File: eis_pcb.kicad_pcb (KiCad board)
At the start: 4 copper layers, 33 x 34.7 mm, 49 parts, among them J1 Conn_01x01_Socket, J12 104031-0811, J13 10051922-1810ELF, J2 GSB1C41110SSHR, J3 Conn_01x01_Socket, J7 Conn_01x02_Socket, Q3 IRLML6344TRPBF, U1 AD5941BCPZ, U3 ESP32-S3-WROOM-1-N8R8, U4 MCP73831T-2DCI_OT, U5 NCP186AMX330TAG

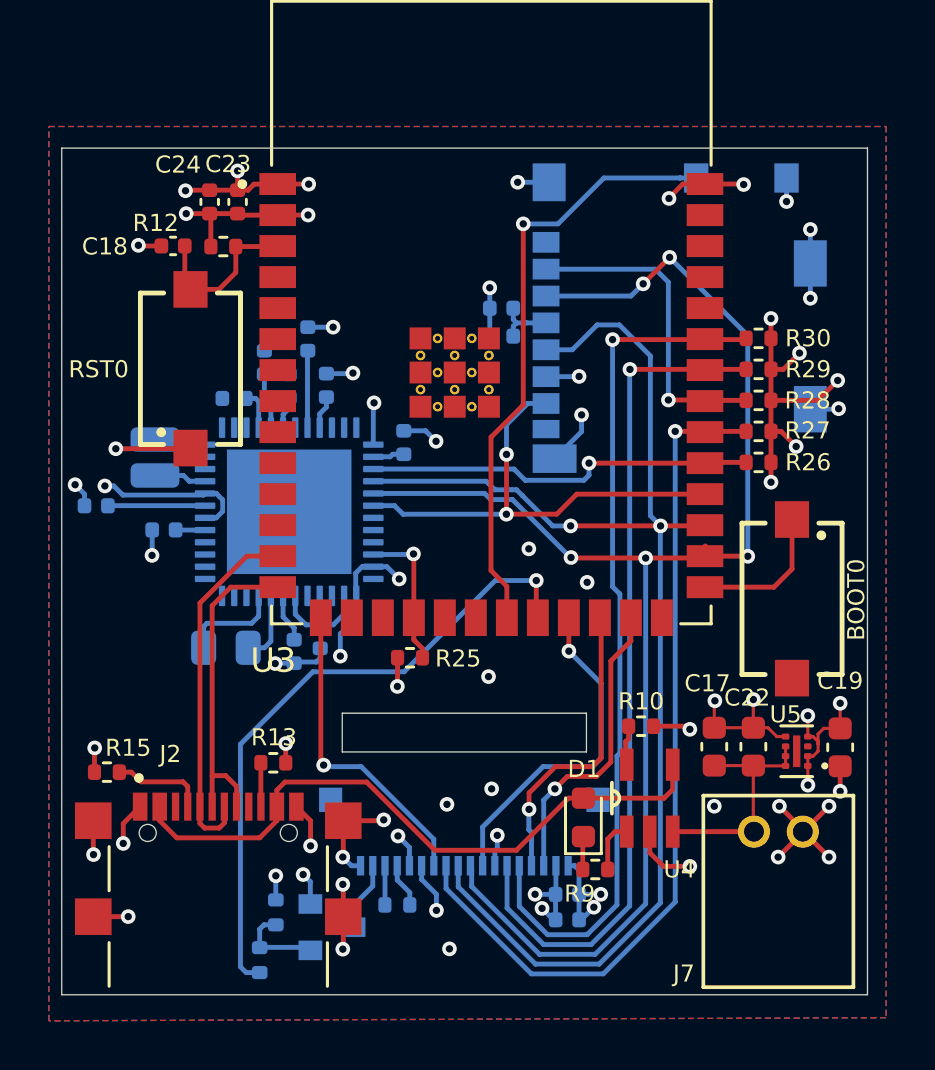
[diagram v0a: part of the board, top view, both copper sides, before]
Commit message: Finished PCB with manufacturing files in production folder
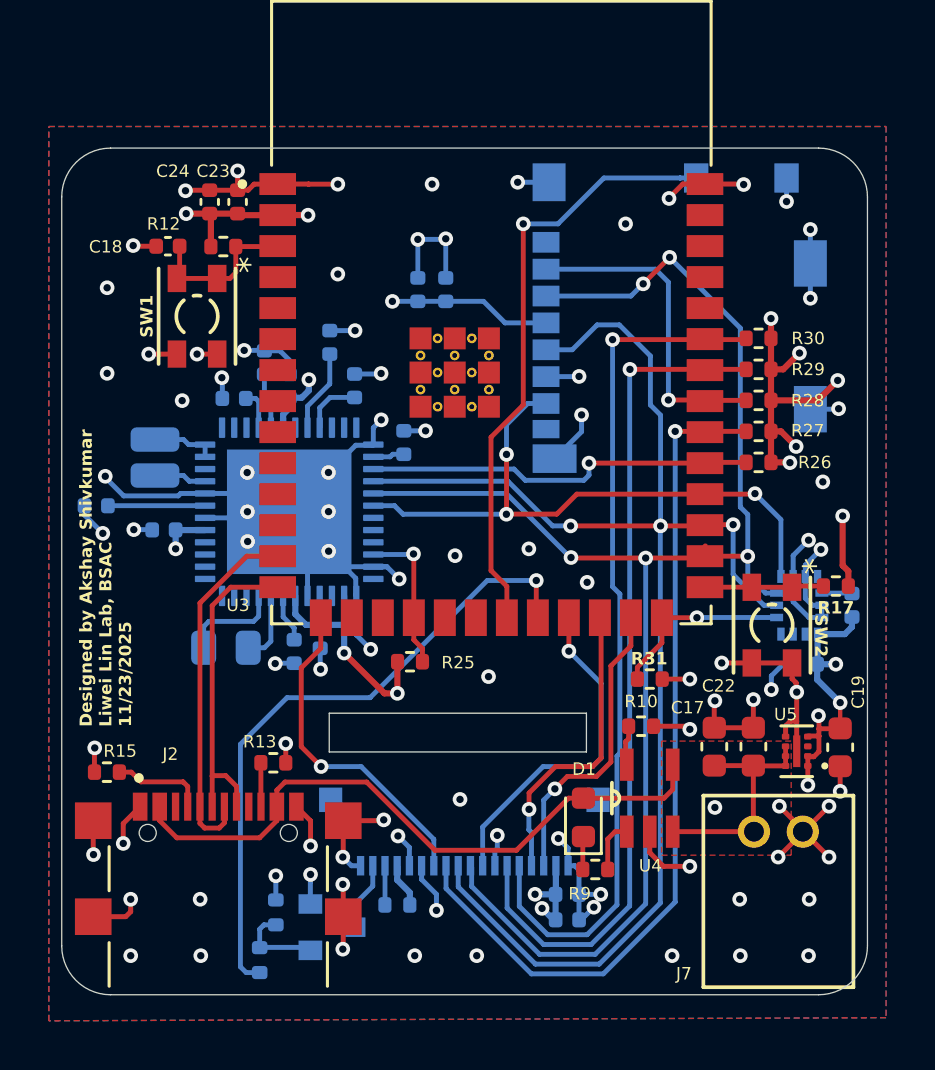
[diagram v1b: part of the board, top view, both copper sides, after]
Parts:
- removed BOOT0, RST0: B3U-1100PM, 434121025816:434121025816
- added C25: 100nF, Capacitor_SMD:C_0402_1005Metric, B.Cu at (139.7, 114.4)
- added C26: 100nF, Capacitor_SMD:C_0402_1005Metric, B.Cu at (141.6, 112.0)
- added R17: 10k, Resistor_SMD:R_0402_1005Metric, F.Cu at (140.9, 111.2)
- added R31: 4.7k, Resistor_SMD:R_0402_1005Metric, F.Cu at (133.3, 115.0)
- added SW1: SW_Push_Dual, SWITCH_0SMTRLFS-L:SWITCH_0SMTRLFS-L, F.Cu at (114.8, 100.2)
- added SW2: SW_Push_Dual, SWITCH_0SMTRLFS-L:SWITCH_0SMTRLFS-L, F.Cu at (138.3, 112.8)
- added U2: LSM6DSVTR, LSM6DSVTR:LGA14-L_2P59X3P1X0P5_STM, B.Cu at (139.4, 112.0)
- moved C11 3.92 mm to (123.8, 99.1), turned to 90 degrees
- moved C12 2.41 mm to (125.0, 99.1), turned to 90 degrees
- moved C10 1.15 mm to (121.2, 103.0)
- moved C9 0.91 mm to (120.2, 101.2)
- moved C18 0.21 mm to (113.6, 97.3)
- moved R25 0.16 mm to (123.5, 114.3)
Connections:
- U3 pad 16: /CS.SCREEN -> unconnected-(U3-IO46-Pad16)
- U3 pad 26: unconnected-(U3-IO45-Pad26) -> /CS.IMU
- U3 pad 32: unconnected-(U3-IO39-Pad32) -> /CS.SCREEN
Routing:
- net GND: track 90.0 -> 143.1 mm, vias 58 -> 91
- net +3V3: track 40.4 -> 60.9 mm, vias 13 -> 20
- net /CS.IMU: track 0.00 -> 7.63 mm, vias 0 -> 1
- net /MISO: track 19.7 -> 25.6 mm, vias 2 -> 3
- net /SCLK: track 54.1 -> 59.6 mm, vias 2 -> 3
- net /MOSI: track 60.0 -> 62.3 mm
- net Net-(U2-VDD_IO): track 0.00 -> 1.24 mm
- net /ZERO.0: track 1.37 -> 2.42 mm
- net /BOOT: track 5.90 -> 4.87 mm
- net /DC: track 12.9 -> 13.7 mm
- added copper zone on In2.Cu, net +3V3
- added copper zone on F.Cu, net +BATT
- added copper zone on In1.Cu, net GND
- removed copper zone on In1.Cu, net +3V3
- removed copper zone on In2.Cu, net GND
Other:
- outline, holes or cut-outs redrawn
- board text added: "Designed by Akshay Shivkumar Liwei Lin Lab, BSAC 11/23/2025"

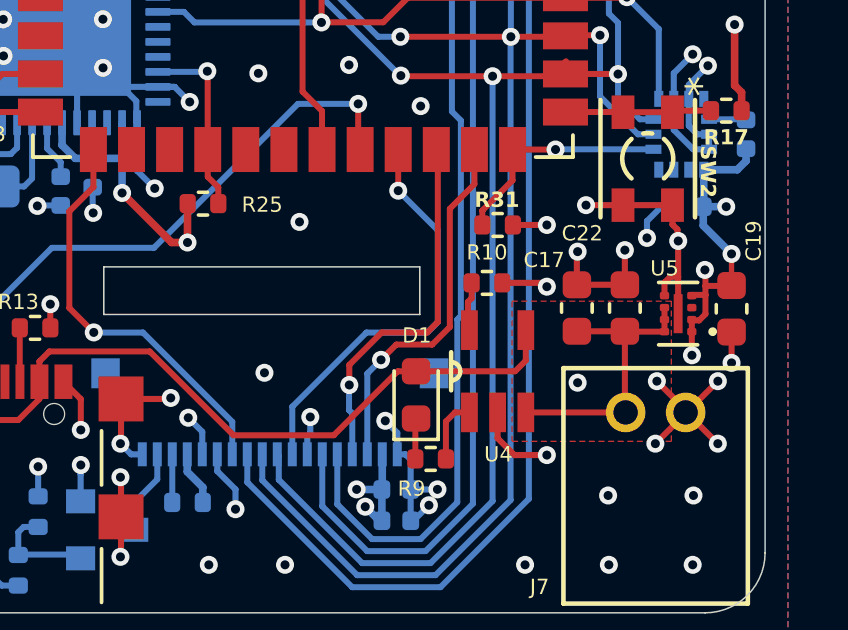
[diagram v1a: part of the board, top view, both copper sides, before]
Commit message: Removed battery zone
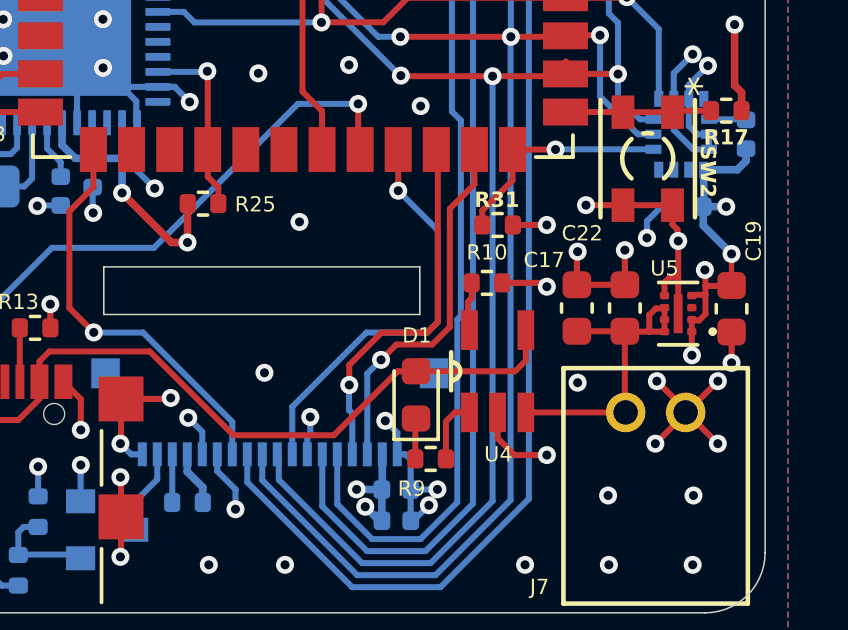
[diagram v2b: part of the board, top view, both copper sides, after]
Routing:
- net +BATT: track 9.85 -> 11.0 mm
- removed copper zone on F.Cu, net +BATT
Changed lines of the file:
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@@
 		(tags "resistor")
 		(property "Reference" "R25"
-			(at -1.9718 -0.036 180)
+			(at -1.7432 -0.0254 180)
 			(layer "F.SilkS")
 			(effects
@@
 	)
 	(segment
+		(start 138.3792 118.0338)
+		(end 138.5944 117.8186)
+		(width 0.2)
+		(layer "F.Cu")
+		(net 11)
+	)
+	(segment
 		(start 138.8872 118.1926)
 		(end 138.8872 118.5926)
@@
 	)
 	(segment
+		(start 138.3792 118.5926)
+		(end 137.5788 118.5926)
+		(width 0.2)
+		(layer "F.Cu")
+		(net 11)
+	)
+	(segment
 		(start 137.5664 121.2596)
 		(end 137.5918 121.285)
@@
 	)
 	(segment
+		(start 138.5944 117.8186)
+		(end 138.8872 117.8186)
+		(width 0.2)
+		(layer "F.Cu")
+		(net 11)
+	)
+	(segment
 		(start 138.8872 118.5926)
-		(end 137.5788 118.5926)
+		(end 138.3792 118.5926)
 		(width 0.2)
 		(layer "F.Cu")
@@
 	)
 	(segment
+		(start 138.3792 118.5926)
+		(end 138.3792 118.0338)
+		(width 0.2)
+		(layer "F.Cu")
+		(net 11)
+	)
+	(segment
 		(start 134.1882 121.285)
 		(end 137.5918 121.285)
@@
 	)
 	(zone
-		(net 11)
-		(net_name "+BATT")
-		(layer "F.Cu")
-		(hatch edge 0.5)
-		(priority 1)
-		(connect_pads
-			(clearance 0.5)
-		)
-		(min_thickness 0.25)
-		(filled_areas_thickness no)
-		(fill yes
-			(thermal_gap 0.5)
-			(thermal_bridge_width 0.5)
-		)
-		(polygon
-			(pts
-				(xy 139.1158 117.5766) (xy 133.8072 117.5766) (xy 133.8072 122.2502) (xy 139.1158 122.2502)
-			)
-		)
-	)
-	(zone

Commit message: Final PCB
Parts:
- U2: value LSM6DSVTR -> LGA14-L_2P59X3P1X0P5_STM; footprint LSM6DSVTR:LGA14-L_2P59X3P1X0P5_STM -> LSM6DSVTR:LGA14-L_2P59X3P1X0P5_STM-L
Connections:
- U2 pad 1: /MISO -> (no net)
- U2 pad 10: unconnected-(U2-OCS_AUX-Pad10) -> (no net)
- U2 pad 11: unconnected-(U2-SDO_AUX-Pad11) -> (no net)
- U2 pad 12: /CS.IMU -> (no net)
- U2 pad 13: /SCLK -> (no net)
- U2 pad 14: /MOSI -> (no net)
- U2 pad 2: GND -> (no net)
- U2 pad 3: GND -> (no net)
- U2 pad 4: unconnected-(U2-INT1-Pad4) -> (no net)
- U2 pad 5: Net-(U2-VDD_IO) -> (no net)
- U2 pad 6: GND -> (no net)
- U2 pad 7: GND -> (no net)
- U2 pad 8: +3V3 -> (no net)
- U2 pad 9: unconnected-(U2-INT2-Pad9) -> (no net)

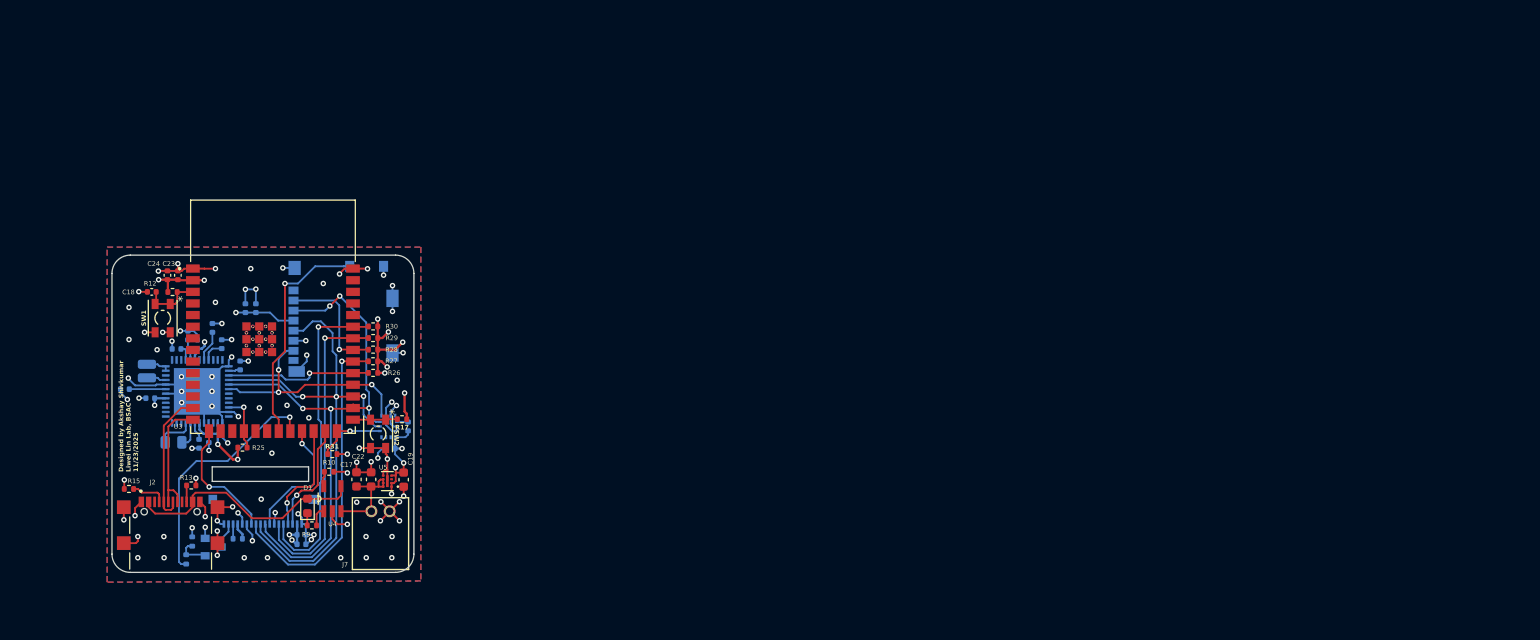
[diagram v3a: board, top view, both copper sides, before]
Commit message: complete noise suppression, begin layout
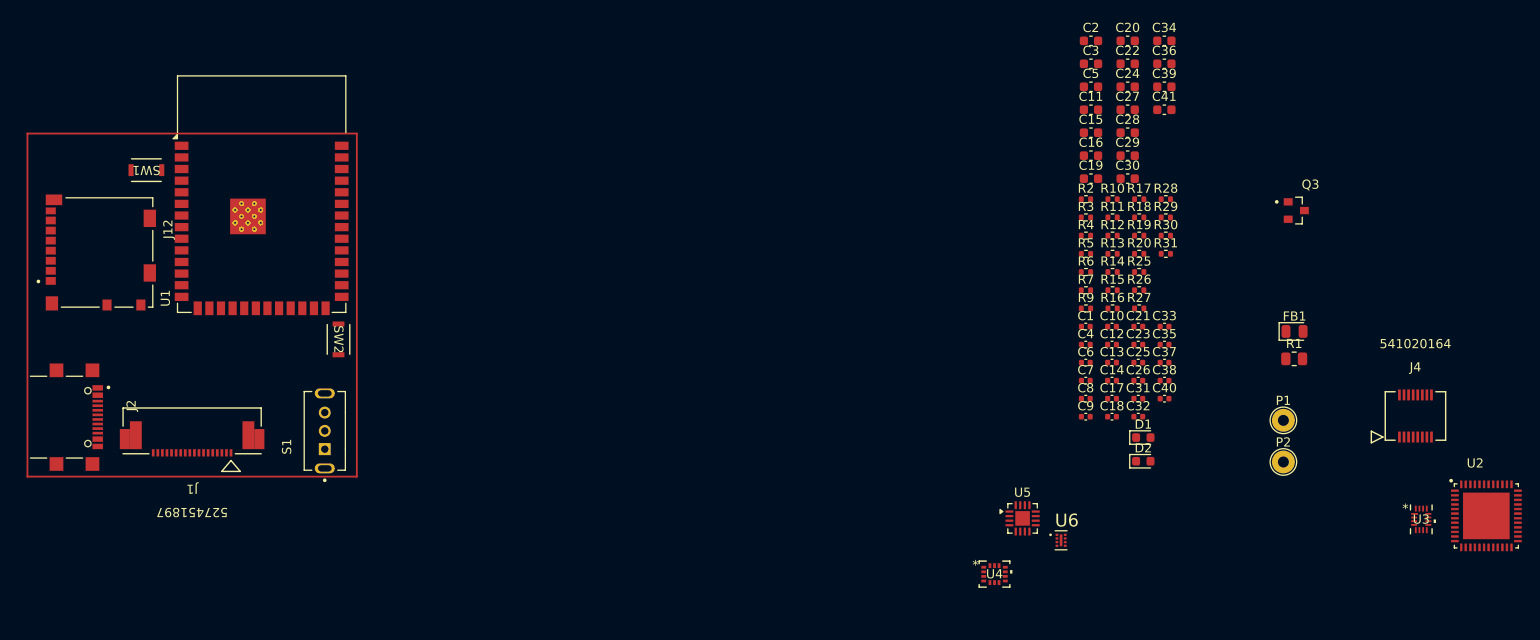
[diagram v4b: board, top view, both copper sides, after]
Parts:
- removed J13: 10051922-1810ELF, 10051922-1810ELF:AMPHENOL_10051922-1810ELF
- removed J3: Conn_01x01_Socket, Connector_Wire:SolderWirePad_1x01_SMD_1x2mm
- removed J7: Conn_01x02_Socket, S2B_PH_K_S_LF__SN_:CONN_S2B-PH-K-S_JST
- added C13: 100n, Capacitor_SMD:C_0402_1005Metric, F.Cu at (218.5, 105.0)
- added C14: 100n, Capacitor_SMD:C_0402_1005Metric, F.Cu at (218.5, 107.0)
- added C15: 1u, Capacitor_SMD:C_0603_1608Metric, F.Cu at (216.2, 79.9)
- added C16: 1u, Capacitor_SMD:C_0603_1608Metric, F.Cu at (216.2, 82.4)
- added C27: 1u, Capacitor_SMD:C_0603_1608Metric, F.Cu at (220.3, 77.4)
- added C28: 4.7u, Capacitor_SMD:C_0603_1608Metric, F.Cu at (220.3, 79.9)
- added C29: 4.7u, Capacitor_SMD:C_0603_1608Metric, F.Cu at (220.3, 82.4)
- added C30: 10u, Capacitor_SMD:C_0603_1608Metric, F.Cu at (220.3, 84.9)
- added C31: 100n, Capacitor_SMD:C_0402_1005Metric, F.Cu at (221.4, 109.0)
- added C32: 100n, Capacitor_SMD:C_0402_1005Metric, F.Cu at (221.4, 110.9)
- added C33: 100n, Capacitor_SMD:C_0402_1005Metric, F.Cu at (224.3, 101.1)
- added C34: 10u, Capacitor_SMD:C_0603_1608Metric, F.Cu at (224.3, 69.9)
- added C35: 100n, Capacitor_SMD:C_0402_1005Metric, F.Cu at (224.3, 103.1)
- added C36: 1u, Capacitor_SMD:C_0603_1608Metric, F.Cu at (224.3, 72.4)
- added C37: 100n, Capacitor_SMD:C_0402_1005Metric, F.Cu at (224.3, 105.0)
- added C38: 100n, Capacitor_SMD:C_0402_1005Metric, F.Cu at (224.3, 107.0)
- added C39: 1u, Capacitor_SMD:C_0603_1608Metric, F.Cu at (224.3, 74.9)
- added C40: 100n, Capacitor_SMD:C_0402_1005Metric, F.Cu at (224.3, 109.0)
- added C41: 1u, Capacitor_SMD:C_0603_1608Metric, F.Cu at (224.3, 77.4)
- added D2: USB, LED_SMD:LED_0603_1608Metric, F.Cu at (222.0, 115.8)
- added FB1: 600R@100MHz, Diode_SMD:D_0805_2012Metric, F.Cu at (238.5, 101.6)
- added J4: 541020164, 541020164:CON_541020164, F.Cu at (251.7, 110.9)
- added P1: V.BATT, TestPoint:TestPoint_THTPad_D2.5mm_Drill1.2mm, F.Cu at (237.3, 111.3)
- added P2: GND.BATT, TestPoint:TestPoint_THTPad_D2.5mm_Drill1.2mm, F.Cu at (237.3, 115.9)
- added R11: 10k, Resistor_SMD:R_0402_1005Metric, F.Cu at (218.6, 89.2)
- added R18: 5.9k, Resistor_SMD:R_0402_1005Metric, F.Cu at (221.5, 89.2)
- added R19: 1.62k, Resistor_SMD:R_0402_1005Metric, F.Cu at (221.5, 91.2)
- added R20: 100k, Resistor_SMD:R_0402_1005Metric, F.Cu at (221.5, 93.1)
- added R3: 220k, Resistor_SMD:R_0402_1005Metric, F.Cu at (215.7, 89.2)
- added R4: 220k, Resistor_SMD:R_0402_1005Metric, F.Cu at (215.7, 91.2)
- added R5: 100k, Resistor_SMD:R_0402_1005Metric, F.Cu at (215.7, 93.1)
- added R6: 2.2R, Resistor_SMD:R_0402_1005Metric, F.Cu at (215.7, 95.1)
- added R7: 2.2R, Resistor_SMD:R_0402_1005Metric, F.Cu at (215.7, 97.1)
- added S1: PWR, SLW_864587_2A_RA_N_D:SW_SLW-864587-2A-RA-N-D, F.Cu at (132.5, 112.5)
- added U6: NCP186AMX330TAG, NCP186AMX330TAG:PSON40P160X120X45-9N, F.Cu at (213.0, 124.5)
- C1, C10, C4, C6, C7, C8, C9, J12, Q3, R1, R14, R16, R2: moved to F.Cu
- C11: value 10uF -> 10u; footprint Capacitor_SMD:C_0402_1005Metric -> Capacitor_SMD:C_0603_1608Metric; moved to F.Cu
- C12, C25, C26: value 100nF -> 100n; moved to F.Cu
- C17: value 10uF -> 100n; footprint Capacitor_SMD:C_0603_1608Metric -> Capacitor_SMD:C_0402_1005Metric
- C18: value 10uF -> 100n
- C19, C23: value 1uF -> 100n
- C2: value 100n -> 1u; footprint Capacitor_SMD:C_0402_1005Metric -> Capacitor_SMD:C_0603_1608Metric; moved to F.Cu
- C20: value 4.7uF -> 4.7u; footprint Capacitor_SMD:C_0402_1005Metric -> Capacitor_SMD:C_0603_1608Metric; moved to F.Cu
- C21: value 0.1uF -> 100n; moved to F.Cu
- C22: value 1uF -> 1u
- C24: value 1uF -> 22u; footprint Capacitor_SMD:C_0402_1005Metric -> Capacitor_SMD:C_0603_1608Metric
- C3: value 100n -> 10u; footprint Capacitor_SMD:C_0402_1005Metric -> Capacitor_SMD:C_0603_1608Metric; moved to F.Cu
- C5: footprint Capacitor_SMD:C_0402_1005Metric -> Capacitor_SMD:C_0603_1608Metric; moved to F.Cu
- D1: value LED -> CHG
- J1: value Conn_01x01_Socket -> 527451897; footprint Connector_Wire:SolderWirePad_1x01_SMD_1x2mm -> 527451897:CON_527451897_MOL; moved to F.Cu
- R10, R9: value 4.7k -> 1.5k
- SW1: value SW_Push_Dual -> RST; footprint SWITCH_0SMTRLFS-L:SWITCH_0SMTRLFS-L -> R_667995:R-667995_MIT
- SW2: value SW_Push_Dual -> BOOT; footprint SWITCH_0SMTRLFS-L:SWITCH_0SMTRLFS-L -> R_667995:R-667995_MIT
- U1: value AD5941BCPZ -> ESP32-S3-WROOM-1-N8R8; footprint AD5941BCPZ:QFN50P700X700X80-49N -> RF_Module:ESP32-S3-WROOM-1; moved to F.Cu
- U2: value LGA14-L_2P59X3P1X0P5_STM -> AD5941BCPZ; footprint LSM6DSVTR:LGA14-L_2P59X3P1X0P5_STM-L -> AD5941BCPZ:QFN50P700X700X80-49N; moved to F.Cu
- U3: value ESP32-S3-WROOM-1-N8R8 -> TMUX1109RSVR; footprint ESP32-S3-WROOM-1-N8R8:XCVR_ESP32S3WROOM1N8R8 -> TMUX1109RSVR:RSV16_TEX
- U4: value MCP73831T-2DCI_OT -> LSM6DSVTR; footprint MCP73831T-2DCI_OT:SOT95P270X145-5N -> LSM6DSVTR:LGA14-L_2P59X3P1X0P5_STM
- U5: value NCP186AMX330TAG -> BQ24075RGT; footprint NCP186AMX330TAG:PSON40P160X120X45-9N -> Package_DFN_QFN:VQFN-16-1EP_3x3mm_P0.5mm_EP1.6x1.6mm
- moved U3 127.5 mm to (252.3, 122.2)
- moved Q3 124.0 mm to (238.7, 88.4)
- moved R1 122.8 mm to (238.5, 104.6), turned to 0 degrees
- moved U2 120.4 mm to (259.5, 121.8), turned to 0 degrees
- moved C5 110.6 mm to (216.2, 74.9), turned to 0 degrees
- moved R15 109.7 mm to (218.6, 97.1), turned to 0 degrees
- moved C3 109.1 mm to (216.2, 72.4), turned to 0 degrees
- moved C24 107.0 mm to (220.3, 74.9), turned to 0 degrees
- moved R2 105.9 mm to (215.7, 87.2), turned to 0 degrees
- moved C18 105.8 mm to (218.5, 110.9), turned to 0 degrees
- moved C20 105.8 mm to (220.3, 69.9)
- moved C2 105.8 mm to (216.2, 69.9), turned to 0 degrees
- moved C23 105.2 mm to (221.4, 103.1), turned to 0 degrees
- moved R14 104.8 mm to (218.6, 95.1), turned to 0 degrees
- moved R13 103.8 mm to (218.6, 93.1)
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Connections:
- C1 pad 1: +3V3 -> Net-(C1-Pad1)
- C17 pad 1: +BATT -> Net-(U2-DVDD)
- C18 pad 1: /MCU.RST -> /RST.MCU
- C2 pad 1: +3V3 -> Net-(C1-Pad1)
- C22 pad 1: +BATT -> +VSYS
- C26 pad 2: Net-(U2-VDD_IO) -> GND
- C3 pad 1: +3V3 -> Net-(C1-Pad1)
- D1 pad 2: +5V -> Net-(D1-A)
- J1 pad 1: /RE -> GND
- Q3 pad 3: /K -> Net-(Q3-Pad3)
- R1 pad 1: Net-(U1-RCAL0) -> Net-(U2-RCAL0)
- R1 pad 2: Net-(U1-RCAL1) -> Net-(U2-RCAL1)
- R10 pad 1: GND -> Net-(D2-A)
- R10 pad 2: Net-(U4-PROG) -> +VSYS
- R12 pad 2: /MCU.RST -> /RST.MCU
- R16 pad 1: +3V3 -> Net-(Q3-Pad3)
- R16 pad 2: Net-(J13-Pad3) -> /K
- R2 pad 1: /ESP.PWM -> /PWM.SCREEN
- R25 pad 1: /AFE.RST -> /RST.AFE
- R27 pad 1: /CS.SCREEN -> Net-(U1-IO39)
- R29 pad 1: /CTP_SCL -> Net-(U1-IO41)
- R30 pad 1: /CTP_SDA -> Net-(U1-IO42)
- R9 pad 1: Net-(D1-K) -> +VSYS
- R9 pad 2: Net-(U4-STAT) -> Net-(D1-A)
- U1 pad 1: unconnected-(U1-RC0_2-Pad1) -> GND
- U1 pad 13: GND -> /DATA-
- U1 pad 14: /DVDD.1V8 -> /DATA+
- U1 pad 15: /CS.AFE -> /SCL.TOUCH
- U1 pad 16: /SCLK -> unconnected-(U1-IO46-Pad16)
- U1 pad 17: /MOSI -> /RST.SCREEN
- U1 pad 18: /MISO -> /CS.SCREEN
- U1 pad 19: unconnected-(U1-GPIO0-Pad19) -> /MOSI.SCREEN
- U1 pad 2: unconnected-(U1-RC0_1-Pad2) -> +3V3
- U1 pad 20: unconnected-(U1-GPIO1-Pad20) -> /SCLK.SCREEN
- U1 pad 21: unconnected-(U1-GPIO2-Pad21) -> /DC.SCREEN
- U1 pad 22: /AFE.RST -> unconnected-(U1-IO14-Pad22)
- U1 pad 23: GND -> /SCREEN.RST
- U1 pad 24: unconnected-(U1-DNC-Pad24) -> /CTP_RST
- U1 pad 25: GND -> /CTP_INT
- U1 pad 26: +3V3 -> /CS.IMU
- U1 pad 27: unconnected-(U1-AFE3-Pad27) -> /BOOT
- U1 pad 29: GND -> unconnected-(U1-IO36-Pad29)
- U1 pad 3: unconnected-(U1-RC0_0-Pad3) -> /RST.MCU
- U1 pad 30: +3V3 -> unconnected-(U1-IO37-Pad30)
- U1 pad 31: /BIAS.CAP -> unconnected-(U1-IO38-Pad31)
- U1 pad 32: Net-(U1-RCAL0) -> Net-(U1-IO39)
- U1 pad 33: Net-(U1-RCAL1) -> /CS.SD
- U1 pad 34: unconnected-(U1-AFE1-Pad34) -> Net-(U1-IO41)
- U1 pad 35: unconnected-(U1-AFE2-Pad35) -> Net-(U1-IO42)
- U1 pad 4: /REF.2V5 -> unconnected-(U1-IO4-Pad4)
- U1 pad 40: unconnected-(U1-AIN4/LPF0-Pad40) -> GND
- U1 pad 41: +3V3 -> (no net)
- U1 pad 5: /AVDD.REG -> unconnected-(U1-IO5-Pad5)
- U1 pad 6: +3V3 -> unconnected-(U1-IO6-Pad6)
- U1 pad 8: /BIAS.0 -> unconnected-(U1-IO15-Pad8)
- U1 pad 9: /ZERO.0 -> unconnected-(U1-IO16-Pad9)
- U2 pad 1: (no net) -> unconnected-(U2-RC0_2-Pad1)
- U2 pad 10: (no net) -> unconnected-(U2-DNC-Pad10)
- U2 pad 11: (no net) -> unconnected-(U2-XTALI-Pad11)
- U2 pad 12: (no net) -> unconnected-(U2-XTALO-Pad12)
- U2 pad 13: (no net) -> GND
- U2 pad 14: (no net) -> /DVDD.1V8
- U2 pad 2: (no net) -> unconnected-(U2-RC0_1-Pad2)
- U2 pad 3: (no net) -> unconnected-(U2-RC0_0-Pad3)
- U2 pad 4: (no net) -> /REF.2V5
- U2 pad 5: (no net) -> /AVDD.REG
- U2 pad 6: (no net) -> Net-(U2-DVDD)
- U2 pad 7: (no net) -> unconnected-(U2-DNC-Pad7)
- U2 pad 8: (no net) -> /BIAS.0
- U2 pad 9: (no net) -> /ZERO.0
- U3 pad 10: unconnected-(U3-IO17-Pad10) -> /WE2
- U3 pad 11: unconnected-(U3-IO18-Pad11) -> /WE1
- U3 pad 12: unconnected-(U3-IO8-Pad12) -> /3V3A
- U3 pad 13: /DATA- -> GND
- U3 pad 14: /DATA+ -> /A1.MUX
- U3 pad 15: /DC -> /A0.MUX
- U3 pad 16: unconnected-(U3-IO46-Pad16) -> /EN.MUX
- U3 pad 2: +3V3 -> /CE1
- U3 pad 3: /MCU.RST -> /CE2
- U3 pad 4: unconnected-(U3-IO4-Pad4) -> /CE3
- U3 pad 5: unconnected-(U3-IO5-Pad5) -> /CE4
- U3 pad 6: unconnected-(U3-IO6-Pad6) -> /CE0
- U3 pad 7: unconnected-(U3-IO7-Pad7) -> /WE0
- U3 pad 8: unconnected-(U3-IO15-Pad8) -> /WE4
- U3 pad 9: unconnected-(U3-IO16-Pad9) -> /WE3
- U4 pad 1: Net-(U4-STAT) -> /MISO
- U4 pad 3: +BATT -> GND
- U4 pad 4: +5V -> /INT.IMU
- U4 pad 5: Net-(U4-PROG) -> +3V3
- U5 pad 1: +3V3 -> Net-(U5-TS)
- U5 pad 2: +3V3 -> +BATT
- U5 pad 3: unconnected-(U5-N/C-Pad3) -> +BATT
- U5 pad 4: +3V3 -> GND
- U5 pad 5: GND -> +VSYS
- U5 pad 6: +BATT -> GND
- U5 pad 7: +BATT -> Net-(D2-K)
- U5 pad 8: +BATT -> GND
- U5 pad 9: GND -> Net-(D1-K)
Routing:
- net GND: track 143.1 -> 0.00 mm, vias 91 -> 0
- net /MOSI: track 62.3 -> 0.00 mm, vias 5 -> 0
- net +3V3: track 60.9 -> 0.00 mm, vias 20 -> 0
- net /SCLK: track 59.6 -> 0.00 mm, vias 3 -> 0
- net /CTP_SDA: track 35.5 -> 0.00 mm, vias 1 -> 0
- net /CS.SCREEN: track 35.2 -> 0.00 mm, vias 1 -> 0
- net /CTP_SCL: track 34.8 -> 0.00 mm, vias 1 -> 0
- net +5V: track 26.8 -> 0.00 mm
- net /ESP.PWM: track 26.4 -> 0.00 mm, vias 1 -> 0
- net /MISO: track 25.6 -> 0.00 mm, vias 3 -> 0
- net /SW1: track 24.8 -> 0.00 mm, vias 1 -> 0
- net /CS.AFE: track 16.1 -> 0.00 mm, vias 1 -> 0
- net /DATA-: track 14.8 -> 0.00 mm
- net /SCREEN.RST: track 13.9 -> 0.00 mm, vias 1 -> 0
- net /DC: track 13.7 -> 0.00 mm, vias 1 -> 0
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- removed copper zone on In2.Cu, net +3V3
- removed copper zone on B.Cu, net GND
- removed copper zone on F.Cu, net GND
- removed copper zone on In1.Cu, net GND
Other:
- board outline removed
- copper layers 4 -> 6
- board text removed: "Designed by Akshay Shivkumar Liwei Lin Lab, BSAC 11/23/2025"
